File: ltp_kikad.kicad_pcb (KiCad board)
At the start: 2 copper layers, 65 x 56.5 mm, 33 parts, among them IC1 SamacSys_Parts_HT16K33-28SOP, IC2 SamacSys_Parts_HT16K33-28SOP, J1 SM04B-SRSS-TB(LF)(SN), J2 RPi_GPIO

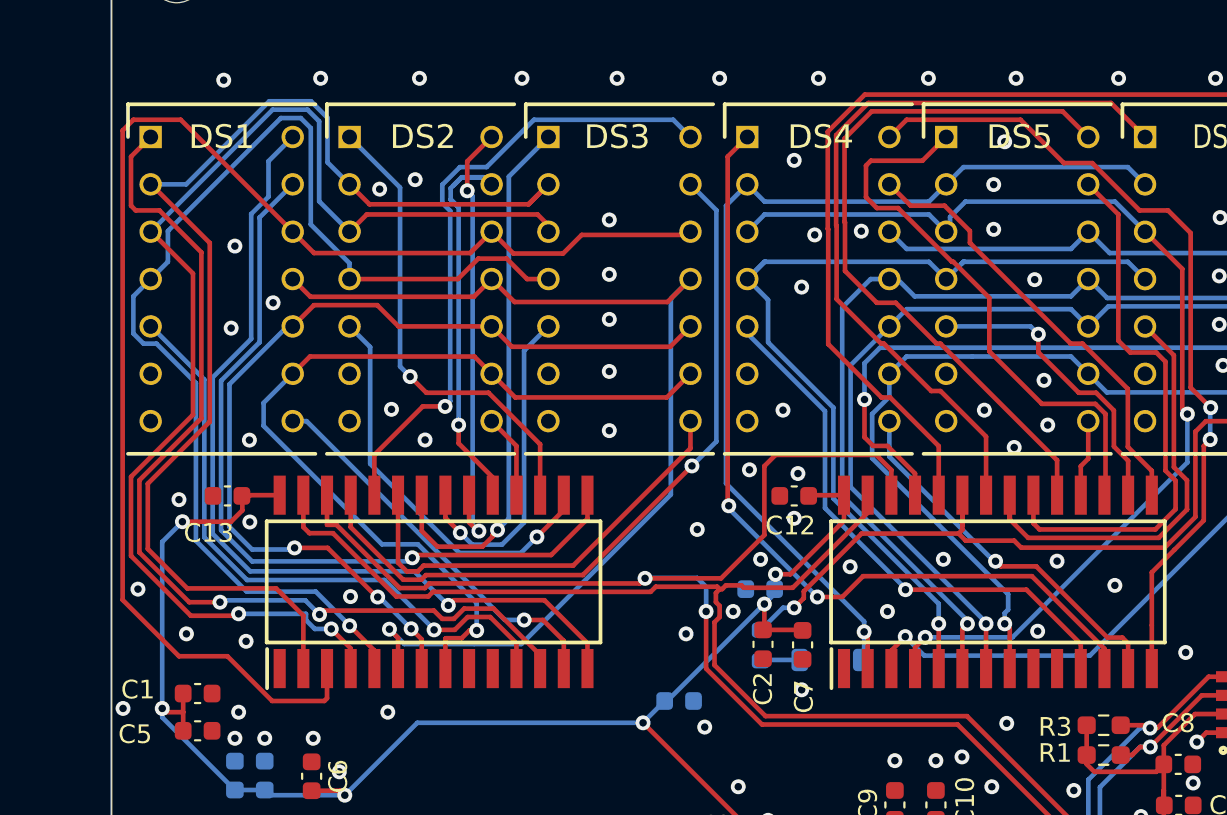
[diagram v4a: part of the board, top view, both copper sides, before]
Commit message: Optimize filled zones, minimize clearence, reroute some led traces
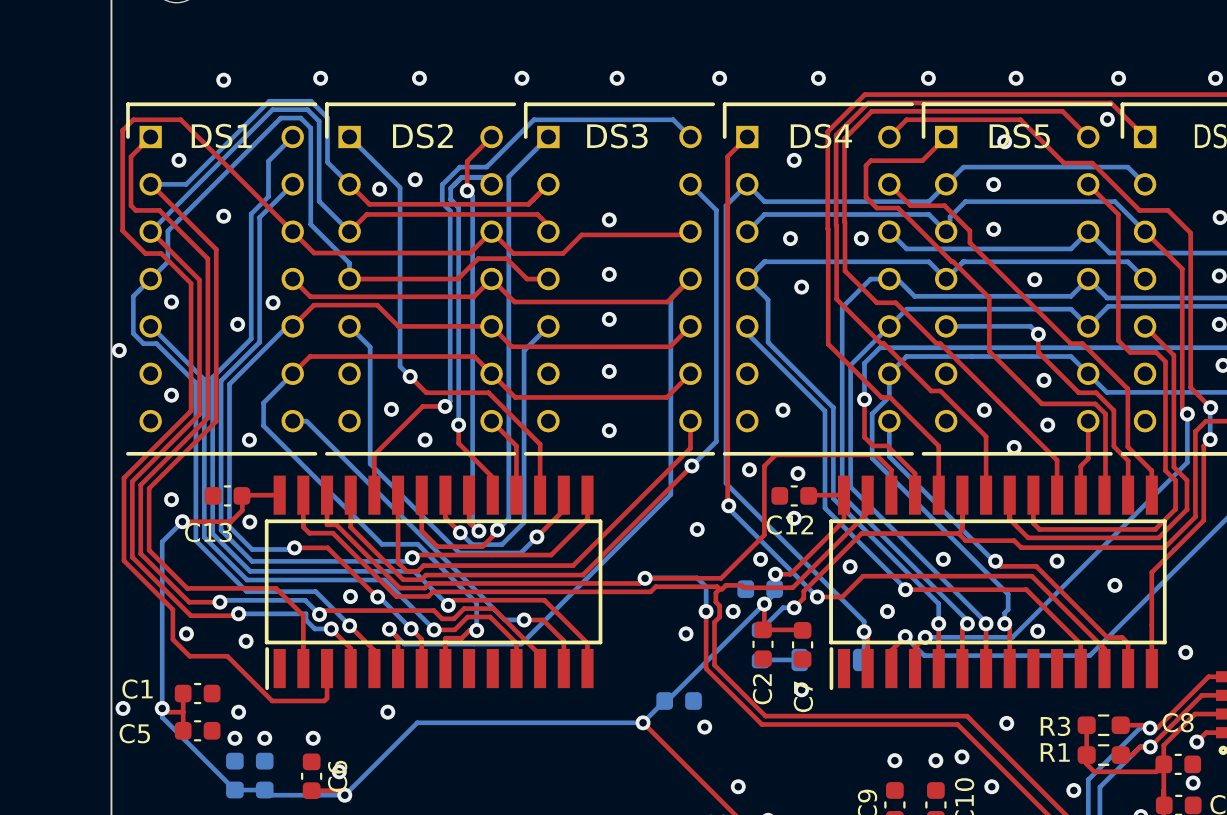
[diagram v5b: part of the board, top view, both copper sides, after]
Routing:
- net ca1: track 75.1 -> 78.3 mm
- net GND: vias 94 -> 98

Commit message: Miscellaneous optimisation
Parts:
- added C16: 10uF, Capacitor_SMD:C_0603_1608Metric, B.Cu at (141.8, 97.4)
- added C17: 10uF, Capacitor_SMD:C_0603_1608Metric, F.Cu at (153.0, 101.2)
- added C18: 10uF, Capacitor_SMD:C_0603_1608Metric, B.Cu at (134.0, 98.8)
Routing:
- net ca0: track 64.0 -> 62.5 mm
- net 2_an8: track 30.4 -> 31.7 mm
- net 2_an3: track 41.1 -> 42.1 mm
- net SCL: track 89.5 -> 88.7 mm
- net 2_an2: track 40.2 -> 40.8 mm
- net 2_an6: track 38.8 -> 39.5 mm
- net 2_an9: track 16.3 -> 16.9 mm
- net 2_an10: track 23.9 -> 24.6 mm
- net 2_ca4: track 49.4 -> 48.8 mm
- net 2_an11: track 44.2 -> 43.7 mm
- net GND: vias 98 -> 101

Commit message: Miscellaneous optimisation
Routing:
- net GND: vias 101 -> 104

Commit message: V 0.01
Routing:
- net ca1: track 78.1 -> 79.1 mm
- net 2_an6: track 39.4 -> 40.1 mm
- net ca2: track 65.5 -> 66.1 mm
- net GND: vias 104 -> 107
